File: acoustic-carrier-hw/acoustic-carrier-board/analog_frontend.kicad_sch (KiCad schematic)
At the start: 31 parts, among them J1 8P8C_Shielded, U3 MS9280

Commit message: added decoupling and power flags
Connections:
- net VDDA: no longer C16.1, C22.1
- net VDD renamed +3.3VA
- new net +3.3V: C16.1, C22.1
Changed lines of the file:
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@@
 	(wire
 		(pts
-			(xy 123.19 113.03) (xy 123.19 114.3)
+			(xy 123.19 111.76) (xy 123.19 114.3)
 		)
 		(stroke
@@
 	(wire
 		(pts
-			(xy 113.03 114.3) (xy 113.03 113.03)
+			(xy 113.03 111.76) (xy 113.03 114.3)
 		)
 		(stroke
@@
 	)
 	(symbol
+		(lib_id "power:+3.3VA")
+		(at 123.19 111.76 0)
+		(unit 1)
+		(exclude_from_sim no)
+		(in_bom yes)
+		(on_board yes)
+		(dnp no)
+		(fields_autoplaced yes)
+		(property "Reference" "#PWR015"
+			(at 123.19 115.57 0)
+			(effects
+				(font
+					(size 1.27 1.27)
+				)
+				(hide yes)
+			)
+		)
+		(property "Value" "+3.3VA"
+			(at 123.19 106.68 0)
+			(effects
+				(font
+					(size 1.27 1.27)
+				)
+			)
+		)
+		(property "Footprint" ""
+			(at 123.19 111.76 0)
+			(effects
+				(font
+					(size 1.27 1.27)
+				)
+				(hide yes)
+			)
+		)
+		(property "Datasheet" ""
+			(at 123.19 111.76 0)
+			(effects
+				(font
+					(size 1.27 1.27)
+				)
+				(hide yes)
+			)
+		)
+		(property "Description" "Power symbol creates a global label with name \"+3.3VA\""
+			(at 123.19 111.76 0)
+			(effects
+				(font
+					(size 1.27 1.27)
+				)
+				(hide yes)
+			)
+		)
+		(pin "1"
+		)
+		(instances
+			(project ""
+				(path "/25b015c9-ab13-4427-b72c-b6f348597100/2e3c577d-8737-43a3-b422-36e75ce65de9"
+					(reference "#PWR015")
+					(unit 1)
+				)
+			)
+		)
+	)
+	(symbol
 		(lib_id "Device:C_Small")
 		(at 35.56 99.06 0)
@@
 	)
 	(symbol
-		(lib_id "power:VDDA")
-		(at 113.03 113.03 0)
-		(unit 1)
-		(exclude_from_sim no)
-		(in_bom yes)
-		(on_board yes)
-		(dnp no)
-		(fields_autoplaced yes)
-		(property "Reference" "#PWR22"
-			(at 113.03 116.84 0)
-			(effects
-				(font
-					(size 1.27 1.27)
-				)
-				(hide yes)
-			)
-		)
-		(property "Value" "VDDA"
-			(at 115.57 111.7599 0)
-			(effects
-				(font
-					(size 1.27 1.27)
-				)
-				(justify left)
-			)
-		)
-		(property "Footprint" ""
-			(at 113.03 113.03 0)
-			(effects
-				(font
-					(size 1.27 1.27)
-				)
-				(hide yes)
-			)
-		)
-		(property "Datasheet" ""
-			(at 113.03 113.03 0)
-			(effects
-				(font
-					(size 1.27 1.27)
-				)
-				(hide yes)
-			)
-		)
-		(property "Description" "Power symbol creates a global label with name \"VDDA\""
-			(at 113.03 113.03 0)
-			(effects
-				(font
-					(size 1.27 1.27)
-				)
-				(hide yes)
-			)
-		)
-		(pin "1"
-		)
-		(instances
-			(project ""
-				(path "/25b015c9-ab13-4427-b72c-b6f348597100/2e3c577d-8737-43a3-b422-36e75ce65de9"
-					(reference "#PWR22")
-					(unit 1)
-				)
-			)
-		)
-	)
-	(symbol
 		(lib_id "Device:C_Small")
 		(at 107.95 118.11 0)
@@
 	)
 	(symbol
+		(lib_id "power:+3.3V")
+		(at 113.03 111.76 0)
+		(unit 1)
+		(exclude_from_sim no)
+		(in_bom yes)
+		(on_board yes)
+		(dnp no)
+		(fields_autoplaced yes)
+		(property "Reference" "#PWR014"
+			(at 113.03 115.57 0)
+			(effects
+				(font
+					(size 1.27 1.27)
+				)
+				(hide yes)
+			)
+		)
+		(property "Value" "+3.3V"
+			(at 113.03 106.68 0)
+			(effects
+				(font
+					(size 1.27 1.27)
+				)
+			)
+		)
+		(property "Footprint" ""
+			(at 113.03 111.76 0)
+			(effects
+				(font
+					(size 1.27 1.27)
+				)
+				(hide yes)
+			)
+		)
+		(property "Datasheet" ""
+			(at 113.03 111.76 0)
+			(effects
+				(font
+					(size 1.27 1.27)
+				)
+				(hide yes)
+			)
+		)
+		(property "Description" "Power symbol creates a global label with name \"+3.3V\""
+			(at 113.03 111.76 0)
+			(effects
+				(font
+					(size 1.27 1.27)
+				)
+				(hide yes)
+			)
+		)
+		(pin "1"
+		)
+		(instances
+			(project ""
+				(path "/25b015c9-ab13-4427-b72c-b6f348597100/2e3c577d-8737-43a3-b422-36e75ce65de9"
+					(reference "#PWR014")
+					(unit 1)
+				)
+			)
+		)
+	)
+	(symbol
 		(lib_id "power:GNDA")
 		(at 146.05 173.99 0)
@@
 					(unit 1)
 				)
-			)
-		)
-	)
-	(symbol
-		(lib_id "power:VDD")
-		(at 123.19 113.03 0)
-		(unit 1)
-		(exclude_from_sim no)
-		(in_bom yes)
-		(on_board yes)
-		(dnp no)
-		(fields_autoplaced yes)
-		(property "Reference" "#PWR23"
-			(at 123.19 116.84 0)
-			(effects
-				(font
-					(size 1.27 1.27)
-				)
-				(hide yes)
-			)
-		)
-		(property "Value" "VDD"
-			(at 125.73 111.7599 0)
-			(effects
-				(font
-					(size 1.27 1.27)
-				)
-				(justify left)
-			)
-		)
-		(property "Footprint" ""
-			(at 123.19 113.03 0)
-			(effects
-				(font
-					(size 1.27 1.27)
-				)
-				(hide yes)
-			)
-		)
-		(property "Datasheet" ""
-			(at 123.19 113.03 0)
-			(effects
-				(font
-					(size 1.27 1.27)
-				)
-				(hide yes)
-			)
-		)
-		(property "Description" "Power symbol creates a global label with name \"VDD\""
-			(at 123.19 113.03 0)
-			(effects
-				(font
-					(size 1.27 1.27)
-				)
-				(hide yes)
-			)
-		)
-		(pin "1"
-		)
-		(instances
-			(project ""
-				(path "/25b015c9-ab13-4427-b72c-b6f348597100/2e3c577d-8737-43a3-b422-36e75ce65de9"
-					(reference "#PWR23")
-					(unit 1)
-				)

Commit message: [carrier] Added decoupling to ethernet PHY
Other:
- note added: "- Differential impedance: 100 ohms - Input capacitance: 300 nF, f_plateau = 1/[2*pi*C*(R_diff/2)] = 30 kHz Max offst: 4% <<<< 1´ @ 1 MHz - Added 0-ohm series resistor in case of single-ended operation (LC damping) TODO: - Think of reusing the same capacitive array twice - (once here once in the ethernet connection)"
- note removed: "- Differential impedance: 100 ohms - Input capacitance: 300 nF, f_plateau = 1/[2*pi*C*(R_diff/2)] = 30 kHz Max offst: 4% <<<< 1´ @ 1 MHz - Added 0-ohm series resistor in case of single-ended operation (LC damping)"
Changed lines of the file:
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@@
 	(generator_version "9.0")
 	(paper "A4")
-	(text "- Differential impedance: 100 ohms\n- Input capacitance: 300 nF, f_plateau = 1/[2*pi*C*(R_diff/2)] = 30 kHz\nMax offst: 4% <<<< 1´ @ 1 MHz\n- Added 0-ohm series resistor in case of single-ended operation (LC damping)"
+	(text "- Differential impedance: 100 ohms\n- Input capacitance: 300 nF, f_plateau = 1/[2*pi*C*(R_diff/2)] = 30 kHz\nMax offst: 4% <<<< 1´ @ 1 MHz\n- Added 0-ohm series resistor in case of single-ended operation (LC damping)\nTODO:\n- Think of reusing the same capacitive array twice \n	- (once here once in the ethernet connection)"
 		(exclude_from_sim no)
 		(at -87.63 69.342 0)
@@
 		)
 		(property "Value" "100 nF +-2%"
-			(at 51.562 73.406 0)
-			(effects
-				(font
+			(at 52.324 80.772 0)
+			(effects
+				(font

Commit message: [carrier] Finished ethernet
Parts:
- C30, C31: value 100 nF +-2% -> 100 nF +-5%; footprint Capacitor_SMD:C_1206_3216Metric_Pad1.33x1.80mm_HandSolder -> Capacitor_SMD:C_0603_1608Metric_Pad1.08x0.95mm_HandSolder; LCSC Part Number C907944 -> C88136; Manufacturing Part Number GRM3195C1H104GA05D -> 0603B104J500NT
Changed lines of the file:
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@@
-	(symbol
-		(lib_id "Device:C_Small")
-		(at 49.53 73.66 90)
-		(unit 1)
-		(exclude_from_sim no)
-		(in_bom yes)
-		(on_board yes)
-		(dnp no)
-		(property "Reference" "C31"
-			(at 48.26 80.264 0)
-			(effects
-				(font
-					(size 1.27 1.27)
-				)
-				(justify left)
-			)
-		)
-		(property "Value" "100 nF +-2%"
-			(at 52.324 80.772 0)
-			(effects
-				(font
-					(size 1.27 1.27)
-				)
-				(justify left)
-			)
-		)
-		(property "Footprint" "Capacitor_SMD:C_1206_3216Metric_Pad1.33x1.80mm_HandSolder"
-			(at 49.53 73.66 0)
-			(effects
-				(font
-					(size 1.27 1.27)
-				)
-				(hide yes)
-			)
-		)
-		(property "Datasheet" "~"
-			(at 49.53 73.66 0)
-			(effects
-				(font
-					(size 1.27 1.27)
-				)
-				(hide yes)
-			)
-		)
-		(property "Description" "Unpolarized capacitor, small symbol"
-			(at 49.53 73.66 0)
-			(effects
-				(font
-					(size 1.27 1.27)
-				)
-				(hide yes)
-			)
-		)
-		(property "LCSC Part Number" "C907944"
-			(at 49.53 73.66 0)
-			(effects
-				(font
-					(size 1.27 1.27)
-				)
-				(hide yes)
-			)
-		)
-		(property "Manufacturing Part Number" "GRM3195C1H104GA05D"
-			(at 49.53 73.66 0)
-			(effects
-				(font
-					(size 1.27 1.27)
-				)
-				(hide yes)
-			)
-		)
-		(pin "2"
-		)
-		(pin "1"
-		)
-		(instances
-			(project "acoustic-characterization-hw"
-				(path "/25b015c9-ab13-4427-b72c-b6f348597100/2e3c577d-8737-43a3-b422-36e75ce65de9"
-					(reference "C31")
-					(unit 1)
-				)
-			)
-		)
-	)
 	(symbol
 		(lib_id "Device:C_Small")
@@
 	)
 	(symbol
+		(lib_id "Device:C_Small")
+		(at 49.53 73.66 90)
+		(unit 1)
+		(exclude_from_sim no)
+		(in_bom yes)
+		(on_board yes)
+		(dnp no)
+		(property "Reference" "C31"
+			(at 48.26 80.264 0)
+			(effects
+				(font
+					(size 1.27 1.27)
+				)
+				(justify left)
+			)
+		)
+		(property "Value" "100 nF +-5%"
+			(at 51.562 73.406 0)
+			(effects
+				(font
+					(size 1.27 1.27)
+				)
+				(justify left)
+			)
+		)
+		(property "Footprint" "Capacitor_SMD:C_0603_1608Metric_Pad1.08x0.95mm_HandSolder"
+			(at 49.53 73.66 0)
+			(effects
+				(font
+					(size 1.27 1.27)
+				)
+				(hide yes)
+			)
+		)
+		(property "Datasheet" "https://jlcpcb.com/api/file/downloadByFileSystemAccessId/8588895711026941952"
+			(at 49.53 73.66 0)
+			(effects
+				(font
+					(size 1.27 1.27)
+				)
+				(hide yes)
+			)
+		)
+		(property "Description" "X7R"
+			(at 49.53 73.66 0)
+			(effects
+				(font
+					(size 1.27 1.27)
+				)
+				(hide yes)
+			)
+		)
+		(property "LCSC Part Number" "C88136"
+			(at 49.53 73.66 0)
+			(effects
+				(font
+					(size 1.27 1.27)
+				)
+				(hide yes)
+			)
+		)
+		(property "Manufacturing Part Number" "0603B104J500NT"
+			(at 49.53 73.66 0)
+			(effects
+				(font
+					(size 1.27 1.27)
+				)
+				(hide yes)
+			)
+		)
+		(pin "2"
+		)
+		(pin "1"
+		)
+		(instances
+			(project "acoustic-carrier-board"
+				(path "/25b015c9-ab13-4427-b72c-b6f348597100/2e3c577d-8737-43a3-b422-36e75ce65de9"
+					(reference "C31")
+					(unit 1)
+				)
+			)
+		)
+	)
+	(symbol
 		(lib_id "power:GNDA")
 		(at 74.93 138.43 0)
@@
 			)
 		)
-		(property "Value" "100 nF +-2%"
+		(property "Value" "100 nF +-5%"
 			(at 51.562 60.706 0)
 			(effects
@@
 			)
 		)
-		(property "Footprint" "Capacitor_SMD:C_1206_3216Metric_Pad1.33x1.80mm_HandSolder"
+		(property "Footprint" "Capacitor_SMD:C_0603_1608Metric_Pad1.08x0.95mm_HandSolder"
 			(at 49.53 60.96 0)
 			(effects
@@
 			)
 		)
-		(property "Datasheet" "~"
+		(property "Datasheet" "https://jlcpcb.com/api/file/downloadByFileSystemAccessId/8588895711026941952"
 			(at 49.53 60.96 0)
 			(effects
@@
 			)
 		)
-		(property "Description" "Unpolarized capacitor, small symbol"
+		(property "Description" "X7R"
 			(at 49.53 60.96 0)
 			(effects
@@
 			)
 		)
-		(property "LCSC Part Number" "C907944"
+		(property "LCSC Part Number" "C88136"
 			(at 49.53 60.96 0)
 			(effects
@@
 			)
 		)
-		(property "Manufacturing Part Number" "GRM3195C1H104GA05D"
+		(property "Manufacturing Part Number" "0603B104J500NT"
 			(at 49.53 60.96 0)
 			(effects

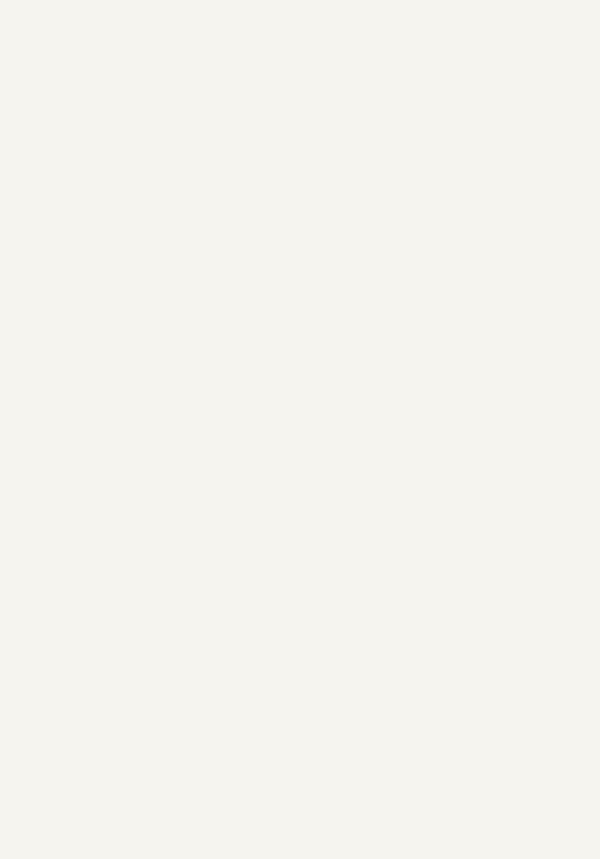
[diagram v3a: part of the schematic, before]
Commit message: [carrier] Added usb power + communication circuitry (next) Connect ADC pins to bank 0, select PWM pins, check connectors for power board
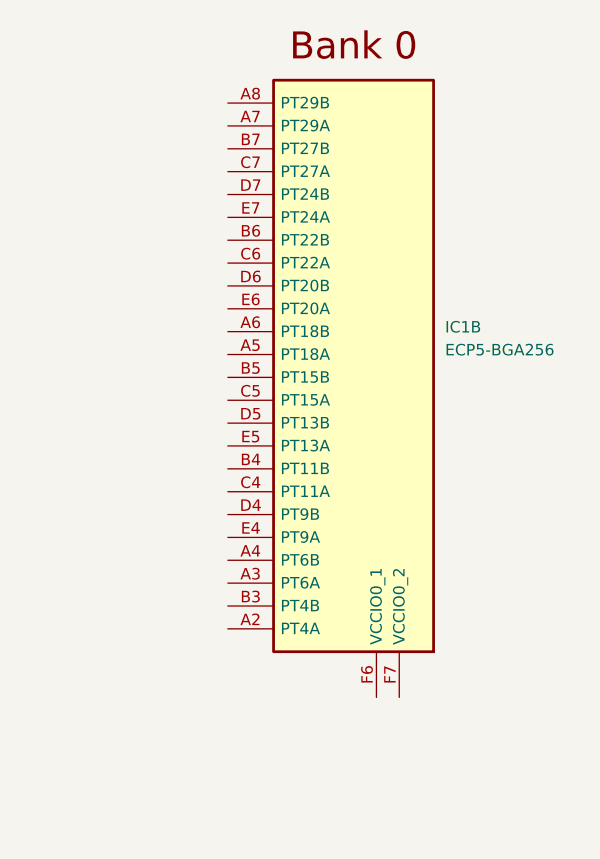
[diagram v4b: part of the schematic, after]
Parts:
- added IC1: ECP5-BGA256, BGA256C80P16X16_1400X1400X170, symbol ecp5bga256:ECP5-BGA256

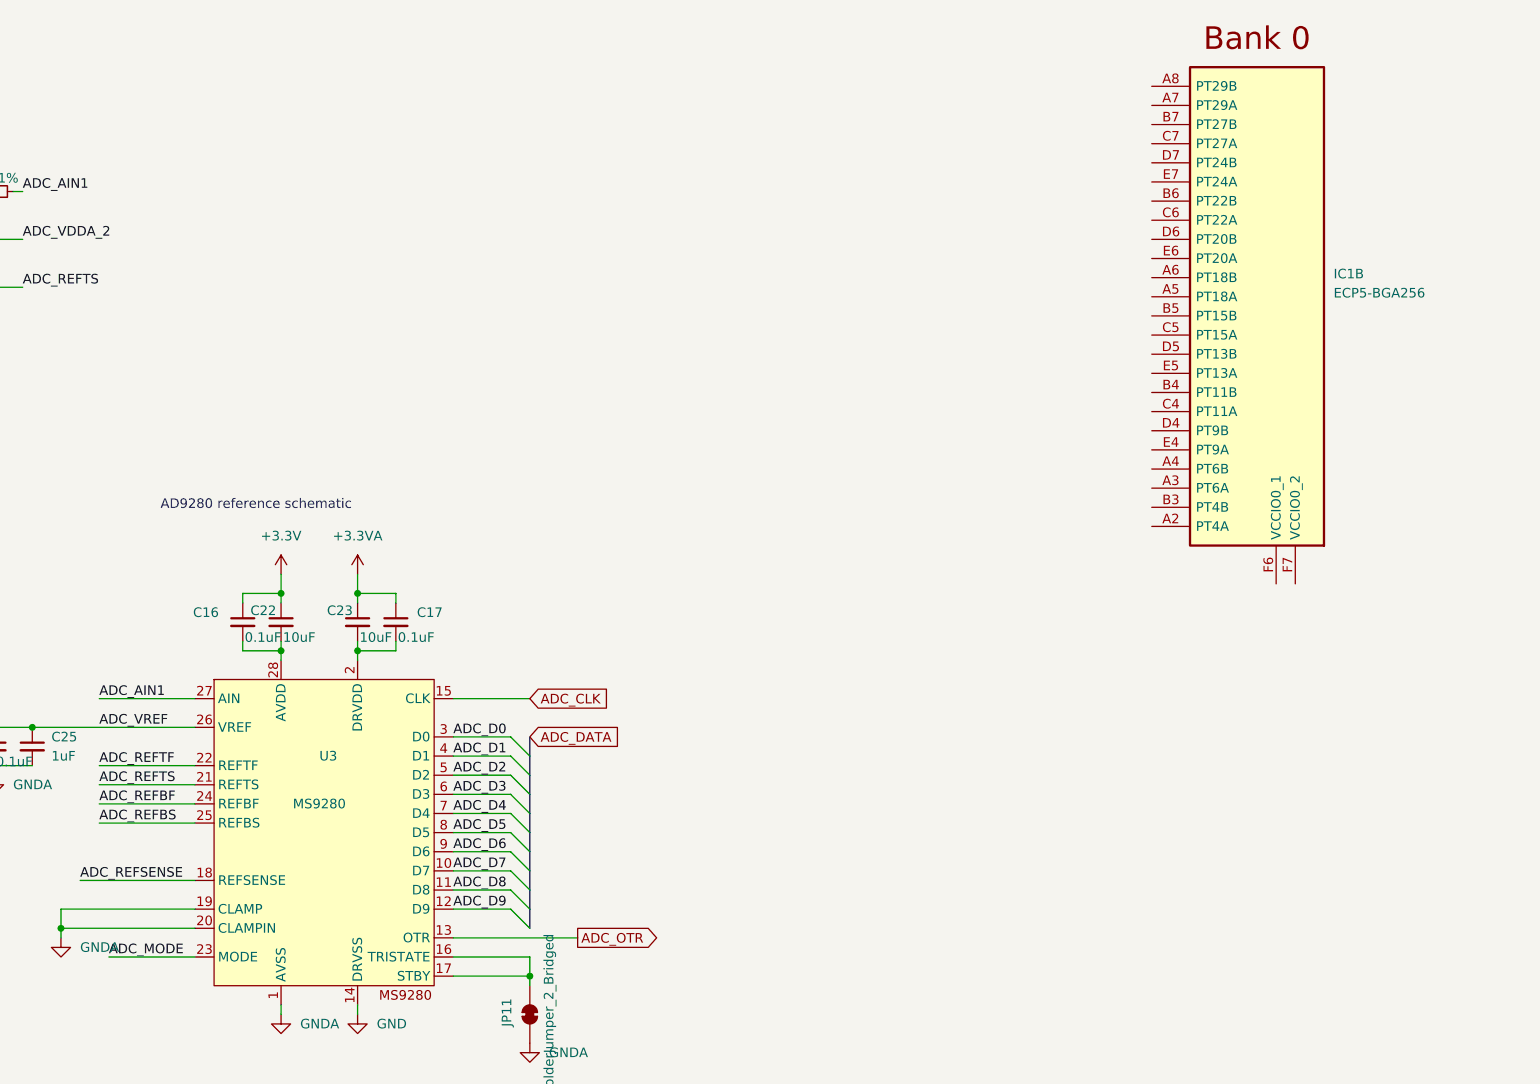
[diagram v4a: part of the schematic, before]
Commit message: [carrier] Finished basic ADC connections (next) decide on connections with power board
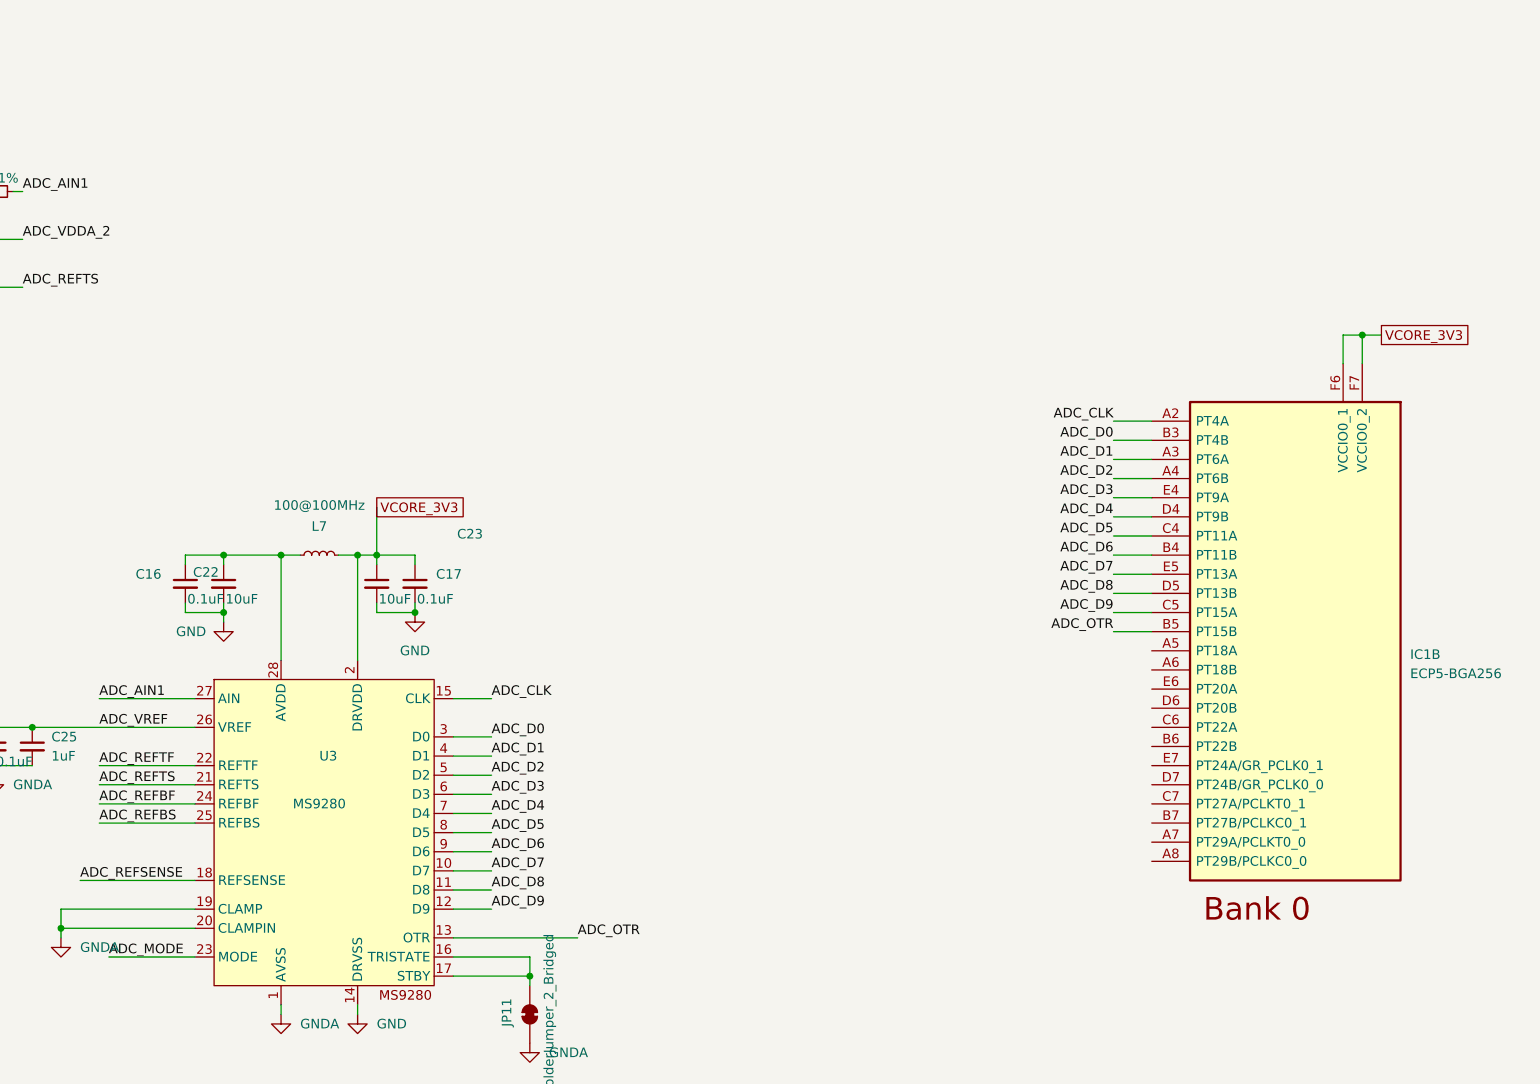
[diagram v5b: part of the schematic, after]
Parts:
- added L7: 100@100MHz, Inductor_SMD:L_0805_2012Metric, symbol Device:L_Small
- U3: LPN (none) -> C1509021; MPN (none) -> MS9280
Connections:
- net +3.3VA is gone; now on net VCORE_3V3: C17.1, C23.1
- net ADC_CLK: now also IC1.A2 (PT4A)
- net ADC_D0: now also IC1.B3 (PT4B)
- net ADC_D1: now also IC1.A3 (PT6A)
- net ADC_D2: now also IC1.A4 (PT6B)
- net ADC_D3: now also IC1.E4 (PT9A)
- net ADC_D4: now also IC1.D4 (PT9B)
- net ADC_D5: now also IC1.C4 (PT11A)
- net ADC_D6: now also IC1.B4 (PT11B)
- net ADC_D7: now also IC1.E5 (PT13A)
- net ADC_D8: now also IC1.D5 (PT13B)
- net ADC_D9: now also IC1.C5 (PT15A)
- net ADC_OTR: now also IC1.B5 (PT15B)
- net GND: now also C16.2, C17.2, C22.2, C23.2
- net VCORE_3V3: now reaches IC1.F6 (VCCIO0_1)
- net VCORE_3V3: now also IC1.F7 (VCCIO0_2), U3.2 (DRVDD), L7.1
- net +3.3V: no longer names the net of C16.1, C22.1
- net +3.3V: now also U3.28 (AVDD), L7.2
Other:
- note removed: "AD9280 reference schematic"
- moved on the sheet: C16, C17, C22, C23, IC1B
